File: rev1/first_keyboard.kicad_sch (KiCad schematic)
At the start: 80 parts, among them SW1 SW_Push, SW10 SW_Push, SW11 SW_Push, SW12 SW_Push, SW13 SW_Push, SW14 SW_Push, SW15 SW_Push, SW16 SW_Push, SW17 SW_Push, SW18 SW_Push, SW19 SW_Push, SW2 SW_Push, SW20 SW_Push, SW21 SW_Push, SW22 SW_Push, SW23 SW_Push, SW24 SW_Push, SW25 SW_Push, SW26 SW_Push, SW27 SW_Push, SW28 SW_Push, SW29 SW_Push, SW3 SW_Push, SW30 SW_Push, SW31 SW_Push, SW32 SW_Push, SW33 SW_Push, SW34 SW_Push, SW35 SW_Push, SW36 SW_Push, SW37 SW_Push, SW38 SW_Push, SW39 SW_Push, SW4 SW_Push, SW40 SW_Push, SW5 SW_Push, SW6 SW_Push, SW7 SW_Push, SW8 SW_Push, SW9 SW_Push, U1 Pico

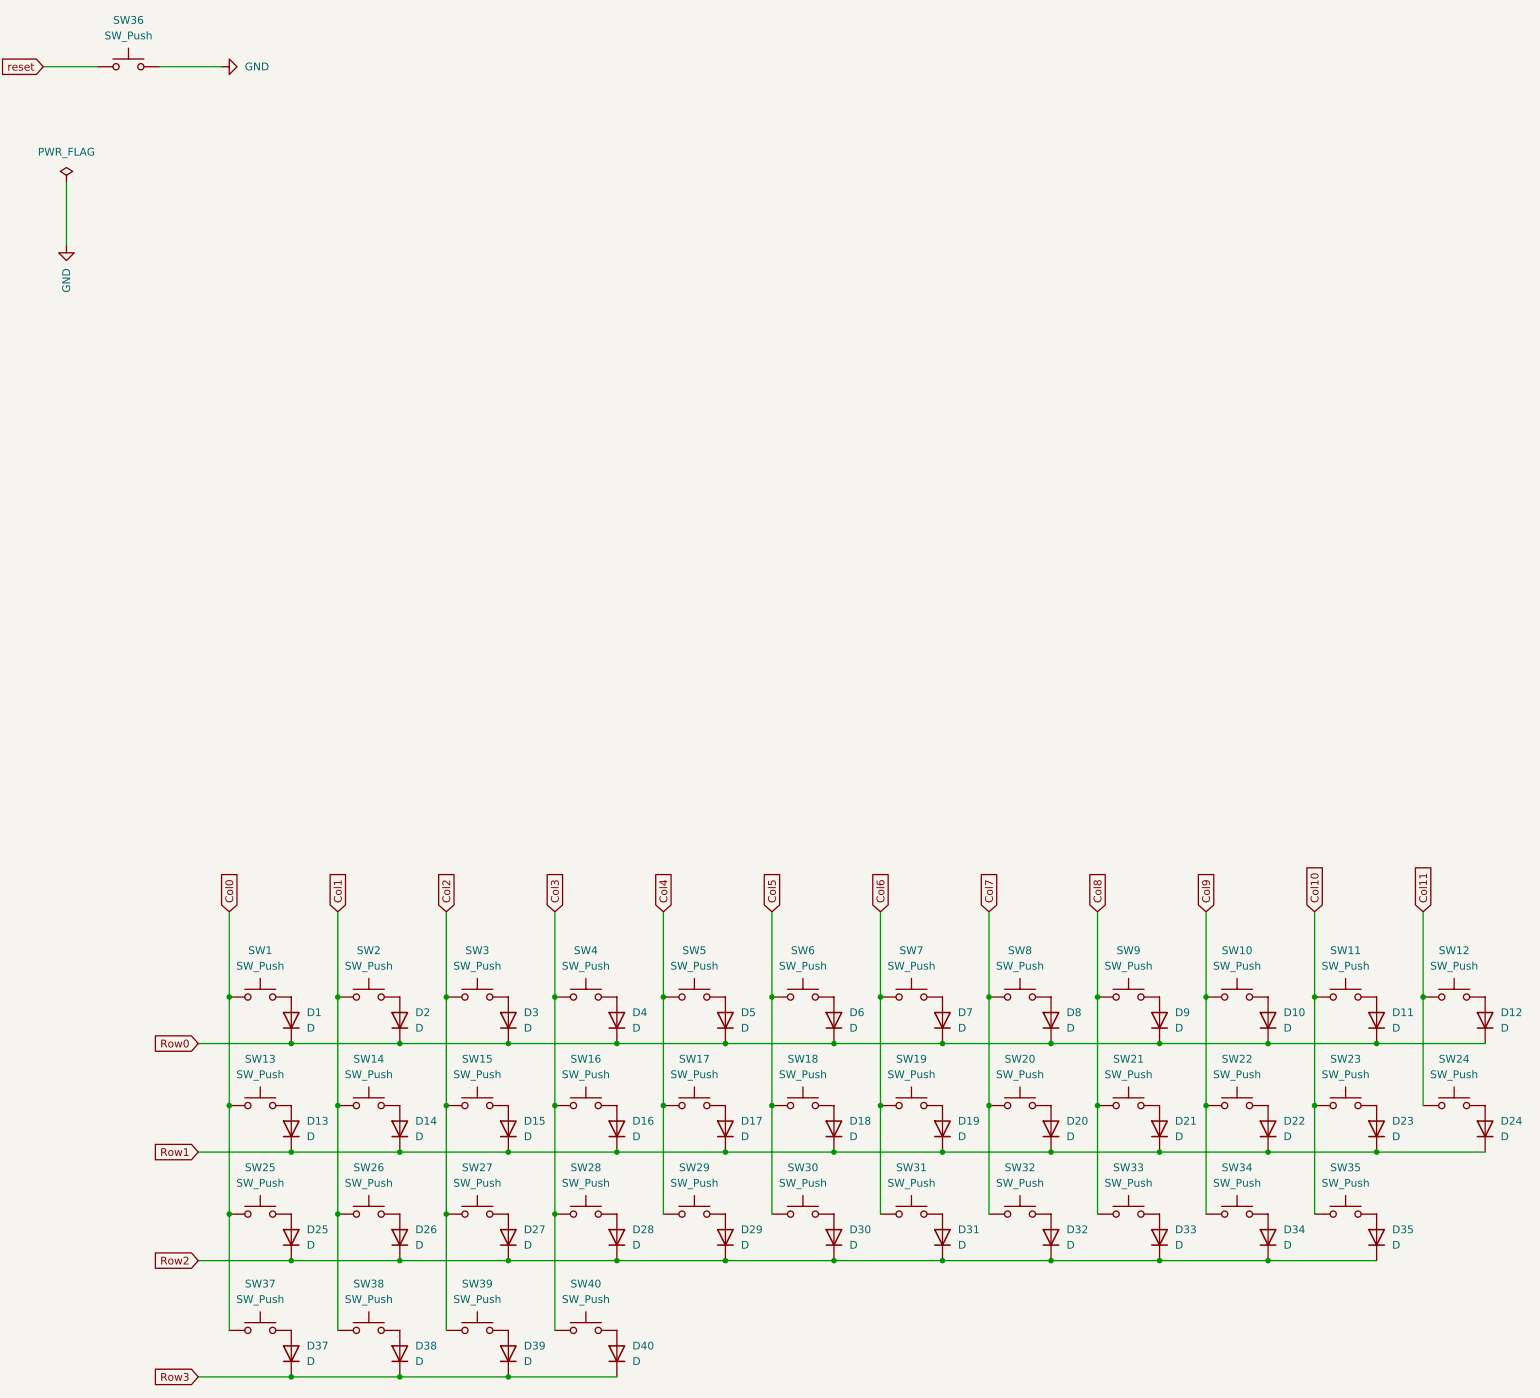
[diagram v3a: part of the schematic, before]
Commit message: feat: ナンバリング修正
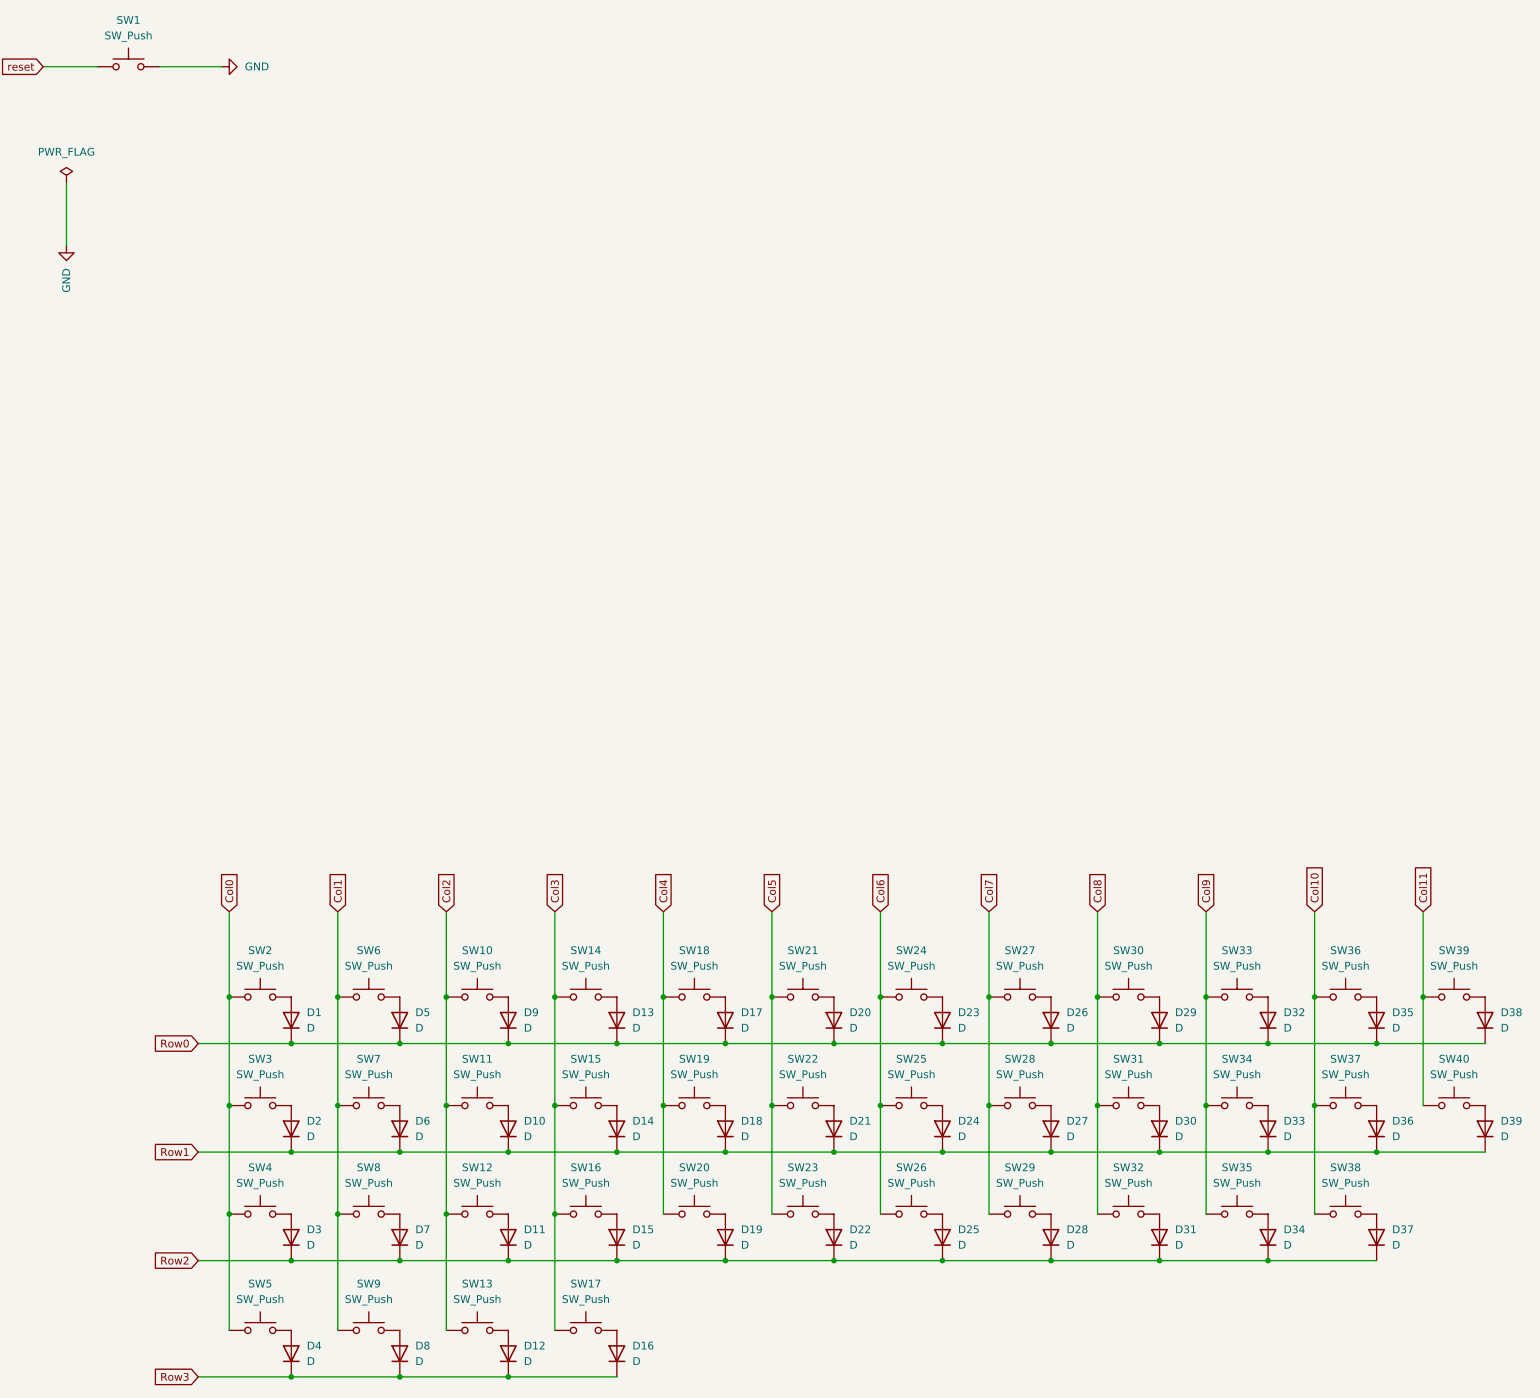
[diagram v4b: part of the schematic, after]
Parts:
- D1, D34: footprint (none) -> kbd_Parts:Diode_TH_SMD
- D10: renamed from D15; footprint (none) -> kbd_Parts:Diode_TH_SMD
- D11: renamed from D27; footprint (none) -> kbd_Parts:Diode_TH_SMD
- D12: renamed from D39; footprint (none) -> kbd_Parts:Diode_TH_SMD
- D13: renamed from D4; footprint (none) -> kbd_Parts:Diode_TH_SMD
- D14: renamed from D16; footprint (none) -> kbd_Parts:Diode_TH_SMD
- D15: renamed from D28; footprint (none) -> kbd_Parts:Diode_TH_SMD
- D16: renamed from D40; footprint (none) -> kbd_Parts:Diode_TH_SMD
- D17: renamed from D5; footprint (none) -> kbd_Parts:Diode_TH_SMD
- D18: renamed from D17; footprint (none) -> kbd_Parts:Diode_TH_SMD
- D19: renamed from D29; footprint (none) -> kbd_Parts:Diode_TH_SMD
- D2: renamed from D13; footprint (none) -> kbd_Parts:Diode_TH_SMD
- D20: renamed from D6; footprint (none) -> kbd_Parts:Diode_TH_SMD
- D21: renamed from D18; footprint (none) -> kbd_Parts:Diode_TH_SMD
- D22: renamed from D30; footprint (none) -> kbd_Parts:Diode_TH_SMD
- D23: renamed from D7; footprint (none) -> kbd_Parts:Diode_TH_SMD
- D24: renamed from D19; footprint (none) -> kbd_Parts:Diode_TH_SMD
- D25: renamed from D31; footprint (none) -> kbd_Parts:Diode_TH_SMD
- D26: renamed from D8; footprint (none) -> kbd_Parts:Diode_TH_SMD
- D27: renamed from D20; footprint (none) -> kbd_Parts:Diode_TH_SMD
- D28: renamed from D32; footprint (none) -> kbd_Parts:Diode_TH_SMD
- D29: renamed from D9; footprint (none) -> kbd_Parts:Diode_TH_SMD
- D3: renamed from D25; footprint (none) -> kbd_Parts:Diode_TH_SMD
- D30: renamed from D21; footprint (none) -> kbd_Parts:Diode_TH_SMD
- D31: renamed from D33; footprint (none) -> kbd_Parts:Diode_TH_SMD
- D32: renamed from D10; footprint (none) -> kbd_Parts:Diode_TH_SMD
- D33: renamed from D22; footprint (none) -> kbd_Parts:Diode_TH_SMD
- D35: renamed from D11; footprint (none) -> kbd_Parts:Diode_TH_SMD
- D36: renamed from D23; footprint (none) -> kbd_Parts:Diode_TH_SMD
- D37: renamed from D35; footprint (none) -> kbd_Parts:Diode_TH_SMD
- D38: renamed from D12; footprint (none) -> kbd_Parts:Diode_TH_SMD
- D39: renamed from D24; footprint (none) -> kbd_Parts:Diode_TH_SMD
- D4: renamed from D37; footprint (none) -> kbd_Parts:Diode_TH_SMD
- D5: renamed from D2; footprint (none) -> kbd_Parts:Diode_TH_SMD
- D6: renamed from D14; footprint (none) -> kbd_Parts:Diode_TH_SMD
- D7: renamed from D26; footprint (none) -> kbd_Parts:Diode_TH_SMD
- D8: renamed from D38; footprint (none) -> kbd_Parts:Diode_TH_SMD
- D9: renamed from D3; footprint (none) -> kbd_Parts:Diode_TH_SMD
- SW1: renamed from SW36; footprint (none) -> kbd_Parts:ResetSW
- SW10: renamed from SW3; footprint (none) -> kbd_SW:CherryMX_Hotswap_1u
- SW11: renamed from SW15; footprint (none) -> kbd_SW:CherryMX_Hotswap_1u
- SW12: renamed from SW27; footprint (none) -> kbd_SW:CherryMX_Hotswap_1u
- SW13: renamed from SW39; footprint (none) -> kbd_SW:CherryMX_Hotswap_1u
- SW14: renamed from SW4; footprint (none) -> kbd_SW:CherryMX_Hotswap_1u
- SW15: renamed from SW16; footprint (none) -> kbd_SW:CherryMX_Hotswap_1u
- SW16: renamed from SW28; footprint (none) -> kbd_SW:CherryMX_Hotswap_1u
- SW17: renamed from SW40; footprint (none) -> kbd_SW:CherryMX_Hotswap_1u
- SW18: renamed from SW5; footprint (none) -> kbd_SW:CherryMX_Hotswap_1u
- SW19: renamed from SW17; footprint (none) -> kbd_SW:CherryMX_Hotswap_1u
- SW2: renamed from SW1; footprint (none) -> kbd_SW:CherryMX_Hotswap_1u
- SW20: renamed from SW29; footprint (none) -> kbd_SW:CherryMX_Hotswap_1u
- SW21: renamed from SW6; footprint (none) -> kbd_SW:CherryMX_Hotswap_1u
- SW22: renamed from SW18; footprint (none) -> kbd_SW:CherryMX_Hotswap_1u
- SW23: renamed from SW30; footprint (none) -> kbd_SW:CherryMX_Hotswap_1u
- SW24: renamed from SW7; footprint (none) -> kbd_SW:CherryMX_Hotswap_1u
- SW25: renamed from SW19; footprint (none) -> kbd_SW:CherryMX_Hotswap_1u
- SW26: renamed from SW31; footprint (none) -> kbd_SW:CherryMX_Hotswap_1u
- SW27: renamed from SW8; footprint (none) -> kbd_SW:CherryMX_Hotswap_1u
- SW28: renamed from SW20; footprint (none) -> kbd_SW:CherryMX_Hotswap_1u
- SW29: renamed from SW32; footprint (none) -> kbd_SW:CherryMX_Hotswap_1u
- SW3: renamed from SW13; footprint (none) -> kbd_SW:CherryMX_Hotswap_1u
- SW30: renamed from SW9; footprint (none) -> kbd_SW:CherryMX_Hotswap_1u
- SW31: renamed from SW21; footprint (none) -> kbd_SW:CherryMX_Hotswap_1u
- SW32: renamed from SW33; footprint (none) -> kbd_SW:CherryMX_Hotswap_1u
- SW33: renamed from SW10; footprint (none) -> kbd_SW:CherryMX_Hotswap_1u
- SW34: renamed from SW22; footprint (none) -> kbd_SW:CherryMX_Hotswap_1u
- SW35: renamed from SW34; footprint (none) -> kbd_SW:CherryMX_Hotswap_1u
- SW36: renamed from SW11; footprint (none) -> kbd_SW:CherryMX_Hotswap_1u
- SW37: renamed from SW23; footprint (none) -> kbd_SW:CherryMX_Hotswap_1u
- SW38: renamed from SW35; footprint (none) -> kbd_SW:CherryMX_Hotswap_1u
- SW39: renamed from SW12; footprint (none) -> kbd_SW:CherryMX_Hotswap_1u
- SW4: renamed from SW25; footprint (none) -> kbd_SW:CherryMX_Hotswap_1u
- SW40: renamed from SW24; footprint (none) -> kbd_SW:CherryMX_Hotswap_1u
- SW5: renamed from SW37; footprint (none) -> kbd_SW:CherryMX_Hotswap_1u
- SW6: renamed from SW2; footprint (none) -> kbd_SW:CherryMX_Hotswap_1u
- SW7: renamed from SW14; footprint (none) -> kbd_SW:CherryMX_Hotswap_1u
- SW8: renamed from SW26; footprint (none) -> kbd_SW:CherryMX_Hotswap_1u
- SW9: renamed from SW38; footprint (none) -> kbd_SW:CherryMX_Hotswap_1u

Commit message: feat: pcbのスイッチ整列\
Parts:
- SW40: footprint kbd_SW:CherryMX_Hotswap_1u -> kbd_SW:CherryMX_Hotswap_2u
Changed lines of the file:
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@@
       (effects (font (size 1.27 1.27)))
     )
-    (property "Footprint" "kbd_SW:CherryMX_Hotswap_1u" (at 328.93 190.5 0)
+    (property "Footprint" "kbd_SW:CherryMX_Hotswap_2u" (at 328.93 190.5 0)
       (effects (font (size 1.27 1.27)) hide)
     )

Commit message: feat:ダイオードの番号降り直しと整列\
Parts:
- renumbered SW2 to SW1, SW11 to SW10, SW12 to SW11, SW13 to SW12, SW14 to SW13, SW15 to SW14, SW16 to SW15, SW17 to SW16, SW18 to SW17, SW19 to SW18, SW20 to SW19, SW3 to SW2, SW21 to SW20, SW22 to SW21, SW23 to SW22, SW24 to SW23, SW25 to SW24, SW26 to SW25, SW27 to SW26, SW28 to SW27, SW29 to SW28, SW30 to SW29, SW4 to SW3, SW31 to SW30, SW32 to SW31, SW33 to SW32, SW34 to SW33, SW35 to SW34, SW36 to SW35, SW37 to SW36, SW38 to SW37, SW39 to SW38, SW40 to SW39, SW5 to SW4, SW1 to SW40, SW6 to SW5, SW7 to SW6, SW8 to SW7, SW9 to SW8, SW10 to SW9
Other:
- moved on the sheet: D1, D10, D11, D12, D13, D14, D15, D16, D17, D18, D19, D2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

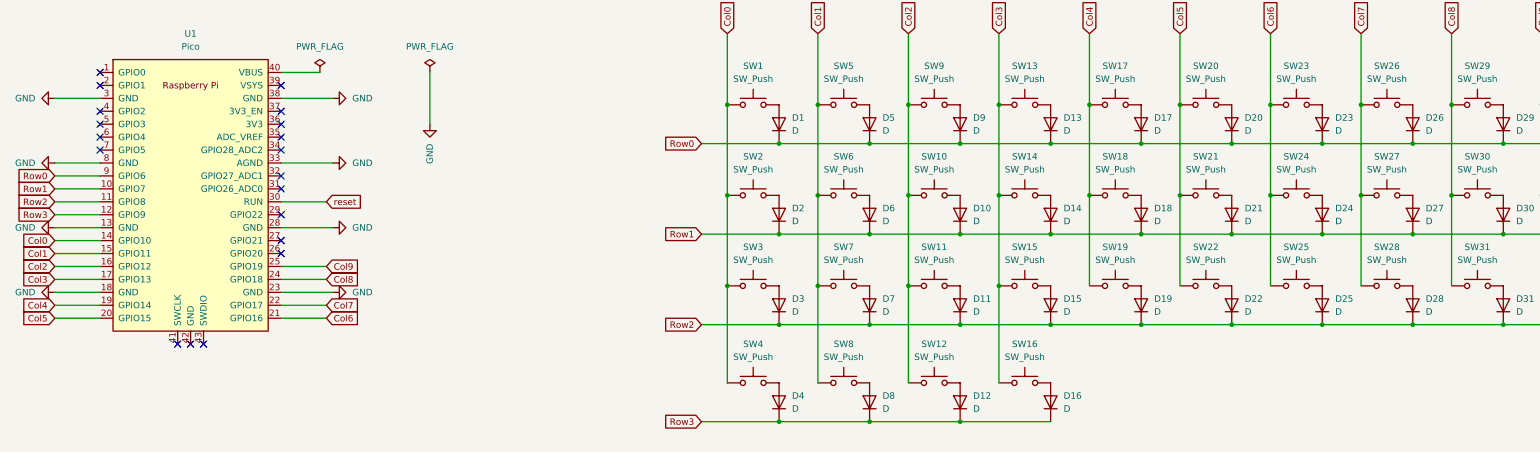
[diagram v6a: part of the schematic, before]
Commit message: feat: ダイオードをスイッチの近くに大移動
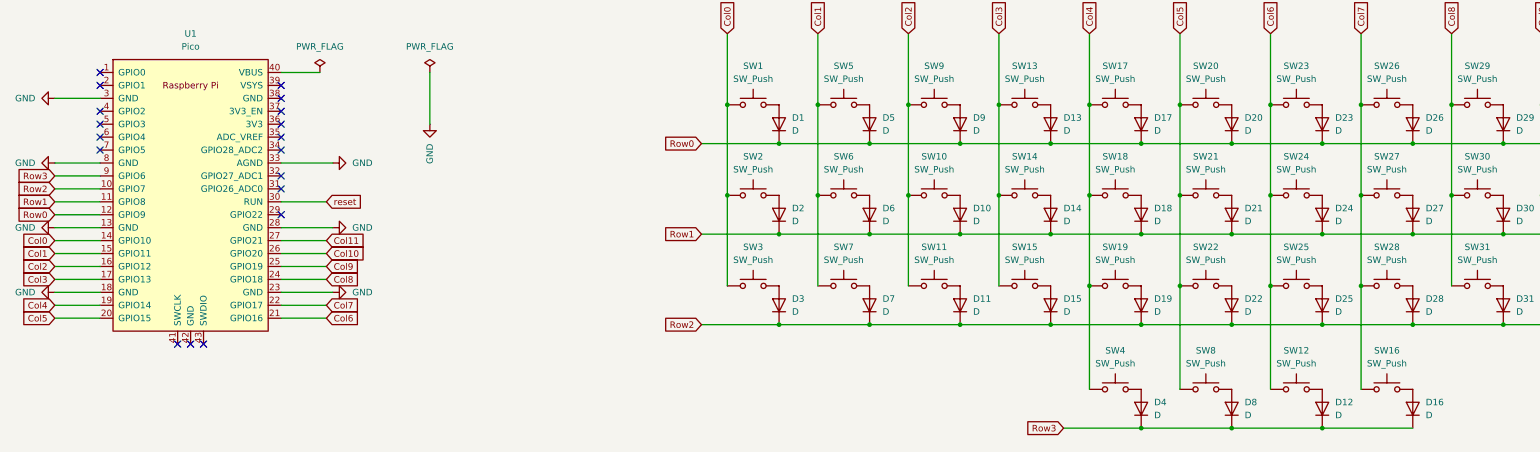
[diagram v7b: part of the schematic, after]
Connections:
- net Col0: no longer SW4.1
- net Col1: no longer SW8.1
- net Col10: now also U1.26 (GPIO20)
- net Col11: now also U1.27 (GPIO21)
- net Col2: no longer SW12.1
- net Col3: no longer SW16.1
- net Col4: now also SW4.1
- net Col5: now also SW8.1
- net Col6: now also SW12.1
- net Col7: now also SW16.1
- net GND: no longer U1.38 (GND)
- net Row0: now also U1.12 (GPIO9); no longer U1.9 (GPIO6)
- net Row1: now also U1.11 (GPIO8); no longer U1.10 (GPIO7)
- net Row2: now also U1.10 (GPIO7); no longer U1.11 (GPIO8)
- net Row3: now also U1.9 (GPIO6); no longer U1.12 (GPIO9)
- no-connect marks 19 -> 18
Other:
- moved on the sheet: D12, D16, D4, D8, SW12, SW16, SW4, SW8

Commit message: fix: ボードの反転を意識してタグを振りなおした
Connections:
- net Col0: now also U1.22 (GPIO17); no longer U1.14 (GPIO10)
- net Col1: now also U1.21 (GPIO16); no longer U1.15 (GPIO11)
- net Col10: now also U1.10 (GPIO7); no longer U1.26 (GPIO20)
- net Col11: now also U1.9 (GPIO6); no longer U1.27 (GPIO21)
- net Col2: now also U1.20 (GPIO15); no longer U1.16 (GPIO12)
- net Col3: now also U1.19 (GPIO14); no longer U1.17 (GPIO13)
- net Col4: now also U1.17 (GPIO13); no longer U1.19 (GPIO14)
- net Col5: now also U1.16 (GPIO12); no longer U1.20 (GPIO15)
- net Col6: now also U1.15 (GPIO11); no longer U1.21 (GPIO16)
- net Col7: now also U1.14 (GPIO10); no longer U1.22 (GPIO17)
- net Col8: now also U1.12 (GPIO9); no longer U1.24 (GPIO18)
- net Col9: now also U1.11 (GPIO8); no longer U1.25 (GPIO19)
- net Row0: now also U1.27 (GPIO21); no longer U1.12 (GPIO9)
- net Row1: now also U1.26 (GPIO20); no longer U1.11 (GPIO8)
- net Row2: now also U1.25 (GPIO19); no longer U1.10 (GPIO7)
- net Row3: now also U1.24 (GPIO18); no longer U1.9 (GPIO6)
